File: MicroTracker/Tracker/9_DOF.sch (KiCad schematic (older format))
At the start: 6 parts

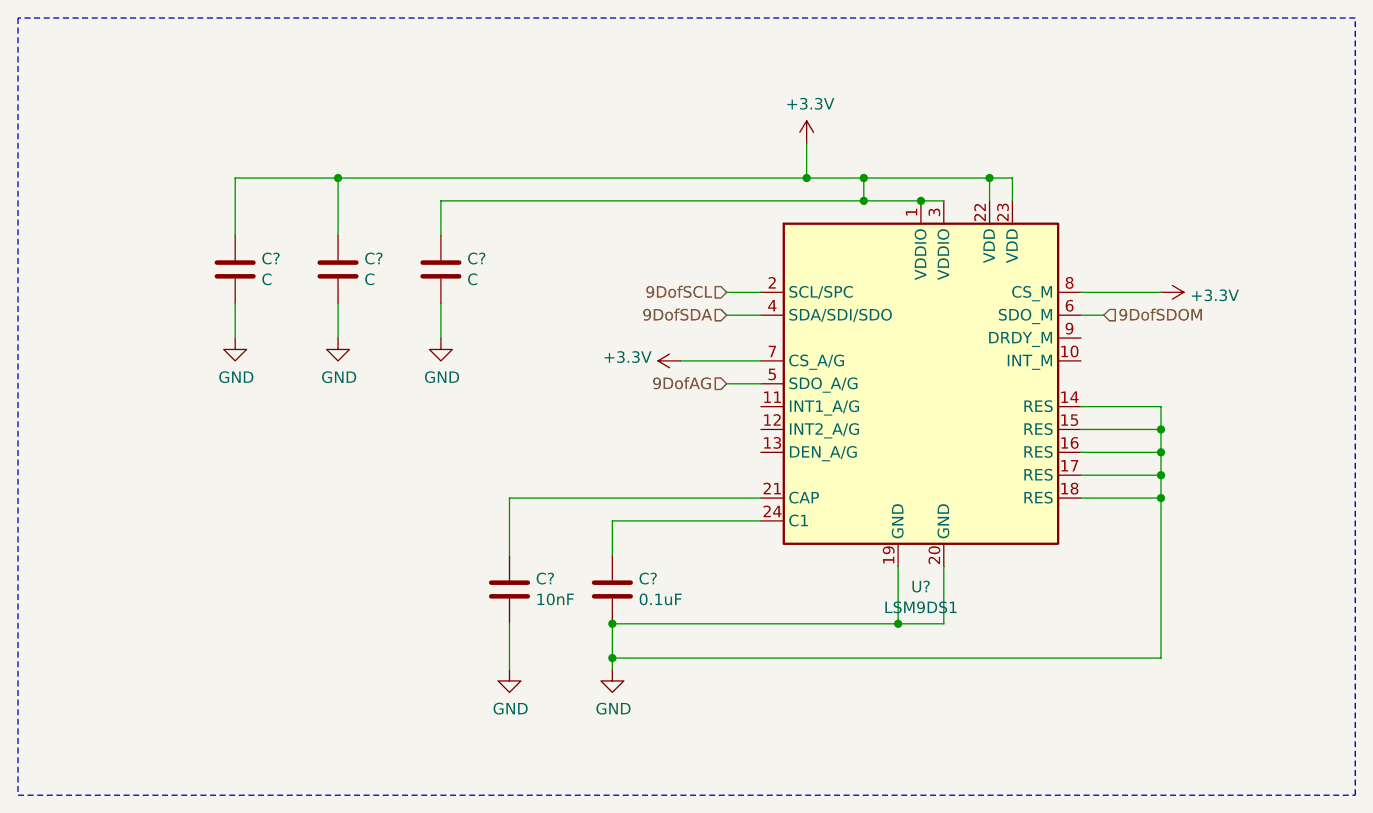
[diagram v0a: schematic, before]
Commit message: added charges
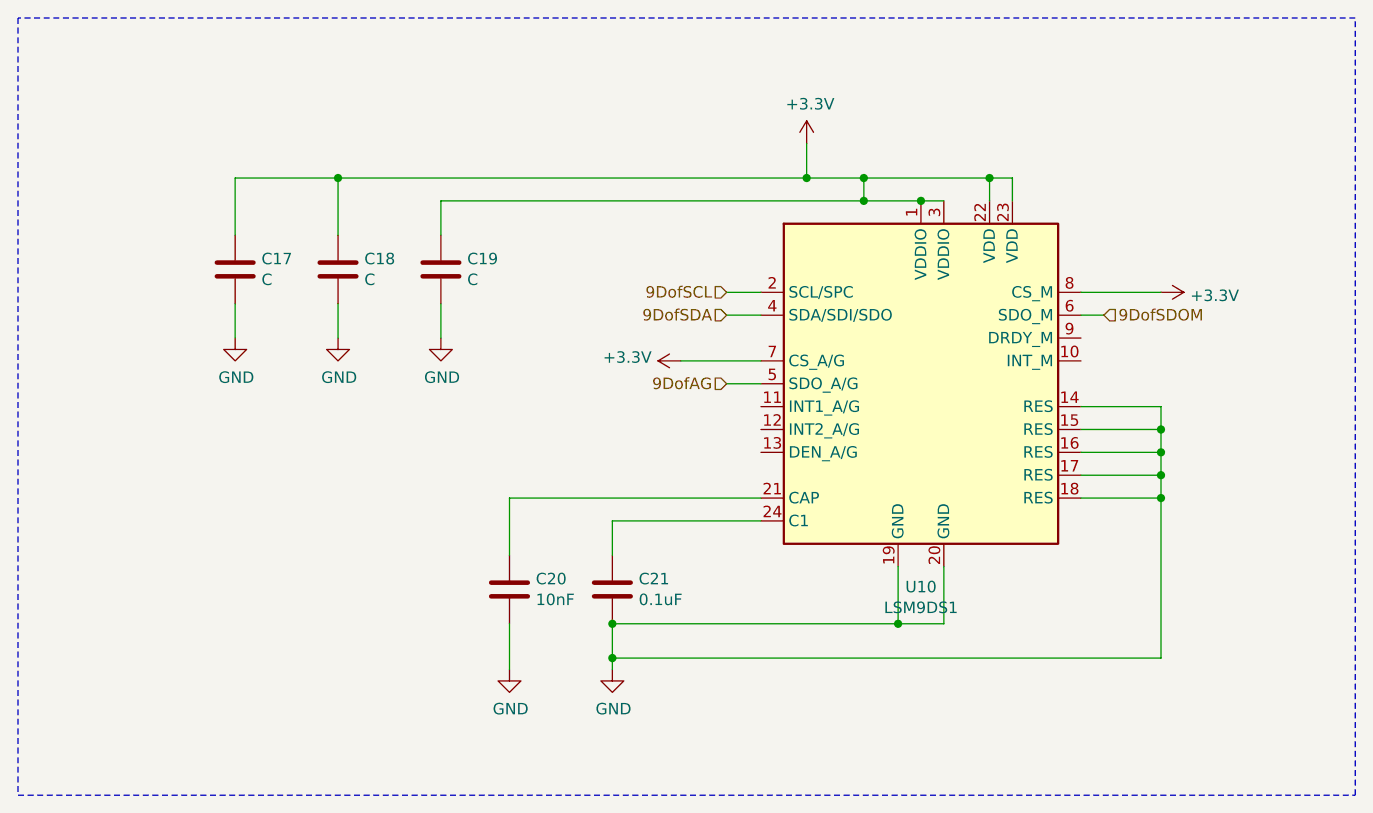
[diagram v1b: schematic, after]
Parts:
- gave numbers to parts that had none: 6
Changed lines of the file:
@@
 $EndDescr
 $Comp
-L Device:C C?
+L Device:C C18
 U 1 1 5F081816
 P 4150 3050
-F 0 "C?" H 4265 3096 50  0000 L CNN
+F 0 "C18" H 4265 3096 50  0000 L CNN
 F 1 "C" H 4265 3005 50  0000 L CNN
 F 2 "" H 4188 2900 50  0001 C CNN
@@
 $EndComp
 $Comp
-L Device:C C?
+L Device:C C19
 U 1 1 5F08223E
 P 4600 3050
-F 0 "C?" H 4715 3096 50  0000 L CNN
+F 0 "C19" H 4715 3096 50  0000 L CNN
 F 1 "C" H 4715 3005 50  0000 L CNN
 F 2 "" H 4638 2900 50  0001 C CNN
@@
 $EndComp
 $Comp
-L Device:C C?
+L Device:C C20
 U 1 1 5F08292F
 P 4900 4450
-F 0 "C?" H 5015 4496 50  0000 L CNN
+F 0 "C20" H 5015 4496 50  0000 L CNN
 F 1 "10nF" H 5015 4405 50  0000 L CNN
 F 2 "" H 4938 4300 50  0001 C CNN
@@
 $EndComp
 $Comp
-L Device:C C?
+L Device:C C21
 U 1 1 5F0833C0
 P 5350 4450
-F 0 "C?" H 5465 4496 50  0000 L CNN
+F 0 "C21" H 5465 4496 50  0000 L CNN
 F 1 "0.1uF" H 5465 4405 50  0000 L CNN
 F 2 "" H 5388 4300 50  0001 C CNN
@@
 $EndComp
 $Comp
-L Device:C C?
+L Device:C C17
 U 1 1 5F0838FF
 P 3700 3050
-F 0 "C?" H 3815 3096 50  0000 L CNN
+F 0 "C17" H 3815 3096 50  0000 L CNN
 F 1 "C" H 3815 3005 50  0000 L CNN
 F 2 "" H 3738 2900 50  0001 C CNN
@@
 	4900 4050 4900 4300
 $Comp
-L power:GND #PWR?
+L power:GND #PWR0157
 U 1 1 5F08A4FA
 P 4900 4800
-F 0 "#PWR?" H 4900 4550 50  0001 C CNN
+F 0 "#PWR0157" H 4900 4550 50  0001 C CNN
 F 1 "GND" H 4905 4627 50  0000 C CNN
 F 2 "" H 4900 4800 50  0001 C CNN
@@
 $EndComp
 $Comp
-L power:GND #PWR?
+L power:GND #PWR0158
 U 1 1 5F08AC1F
 P 5350 4800
-F 0 "#PWR?" H 5350 4550 50  0001 C CNN
+F 0 "#PWR0158" H 5350 4550 50  0001 C CNN
 F 1 "GND" H 5355 4627 50  0000 C CNN
 F 2 "" H 5350 4800 50  0001 C CNN
@@
 	6000 4150 5350 4150
 $Comp
-L Sensor_Motion:LSM9DS1 U?
+L Sensor_Motion:LSM9DS1 U10
 U 1 1 5F07FF21
 P 6700 3550
-F 0 "U?" H 6700 2661 50  0000 C CNN
+F 0 "U10" H 6700 2661 50  0000 C CNN
 F 1 "LSM9DS1" H 6700 2570 50  0000 C CNN
 F 2 "Package_LGA:LGA-24L_3x3.5mm_P0.43mm" H 8200 4300 50  0001 C CNN
@@
 	6600 4600 5350 4600
 $Comp
-L power:+3.3V #PWR?
+L power:+3.3V #PWR0159
 U 1 1 5F08DE33
 P 7750 3150
-F 0 "#PWR?" H 7750 3000 50  0001 C CNN
+F 0 "#PWR0159" H 7750 3000 50  0001 C CNN
 F 1 "+3.3V" V 7765 3278 50  0000 L CNN
 F 2 "" H 7750 3150 50  0001 C CNN
@@
 	7400 3150 7750 3150
 $Comp
-L power:+3.3V #PWR?
+L power:+3.3V #PWR0160
 U 1 1 5F090E2F
 P 5650 3450
-F 0 "#PWR?" H 5650 3300 50  0001 C CNN
+F 0 "#PWR0160" H 5650 3300 50  0001 C CNN
 F 1 "+3.3V" V 5665 3578 50  0000 L CNN
 F 2 "" H 5650 3450 50  0001 C CNN
@@
 	4150 2650 3700 2650
 $Comp
-L power:GND #PWR?
+L power:GND #PWR0161
 U 1 1 5F099576
 P 4600 3350
-F 0 "#PWR?" H 4600 3100 50  0001 C CNN
+F 0 "#PWR0161" H 4600 3100 50  0001 C CNN
 F 1 "GND" H 4605 3177 50  0000 C CNN
 F 2 "" H 4600 3350 50  0001 C CNN
@@
 $EndComp
 $Comp
-L power:GND #PWR?
+L power:GND #PWR0162
 U 1 1 5F099C04
 P 4150 3350
-F 0 "#PWR?" H 4150 3100 50  0001 C CNN
+F 0 "#PWR0162" H 4150 3100 50  0001 C CNN
 F 1 "GND" H 4155 3177 50  0000 C CNN
 F 2 "" H 4150 3350 50  0001 C CNN
@@
 $EndComp
 $Comp
-L power:GND #PWR?
+L power:GND #PWR0163
 U 1 1 5F09A29E
 P 3700 3350
-F 0 "#PWR?" H 3700 3100 50  0001 C CNN
+F 0 "#PWR0163" H 3700 3100 50  0001 C CNN
 F 1 "GND" H 3705 3177 50  0000 C CNN
 F 2 "" H 3700 3350 50  0001 C CNN
@@
 	6450 2650 6200 2650
 $Comp
-L power:+3.3V #PWR?
+L power:+3.3V #PWR0164
 U 1 1 5F09D5DF
 P 6200 2500
-F 0 "#PWR?" H 6200 2350 50  0001 C CNN
+F 0 "#PWR0164" H 6200 2350 50  0001 C CNN
 F 1 "+3.3V" H 6215 2673 50  0000 C CNN
 F 2 "" H 6200 2500 50  0001 C CNN

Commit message: assigned parts
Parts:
- C17, C18, C19, C20, C21: footprint (none) -> Capacitor_SMD:C_0805_2012Metric_Pad1.15x1.40mm_HandSolder
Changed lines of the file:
@@
 F 0 "C18" H 4265 3096 50  0000 L CNN
 F 1 "C" H 4265 3005 50  0000 L CNN
-F 2 "" H 4188 2900 50  0001 C CNN
+F 2 "Capacitor_SMD:C_0805_2012Metric_Pad1.15x1.40mm_HandSolder" H 4188 2900 50  0001 C CNN
 F 3 "~" H 4150 3050 50  0001 C CNN
 	1    4150 3050
@@
 F 0 "C19" H 4715 3096 50  0000 L CNN
 F 1 "C" H 4715 3005 50  0000 L CNN
-F 2 "" H 4638 2900 50  0001 C CNN
+F 2 "Capacitor_SMD:C_0805_2012Metric_Pad1.15x1.40mm_HandSolder" H 4638 2900 50  0001 C CNN
 F 3 "~" H 4600 3050 50  0001 C CNN
 	1    4600 3050
@@
 F 0 "C20" H 5015 4496 50  0000 L CNN
 F 1 "10nF" H 5015 4405 50  0000 L CNN
-F 2 "" H 4938 4300 50  0001 C CNN
+F 2 "Capacitor_SMD:C_0805_2012Metric_Pad1.15x1.40mm_HandSolder" H 4938 4300 50  0001 C CNN
 F 3 "~" H 4900 4450 50  0001 C CNN
 	1    4900 4450
@@
 F 0 "C21" H 5465 4496 50  0000 L CNN
 F 1 "0.1uF" H 5465 4405 50  0000 L CNN
-F 2 "" H 5388 4300 50  0001 C CNN
+F 2 "Capacitor_SMD:C_0805_2012Metric_Pad1.15x1.40mm_HandSolder" H 5388 4300 50  0001 C CNN
 F 3 "~" H 5350 4450 50  0001 C CNN
 	1    5350 4450
@@
 F 0 "C17" H 3815 3096 50  0000 L CNN
 F 1 "C" H 3815 3005 50  0000 L CNN
-F 2 "" H 3738 2900 50  0001 C CNN
+F 2 "Capacitor_SMD:C_0805_2012Metric_Pad1.15x1.40mm_HandSolder" H 3738 2900 50  0001 C CNN
 F 3 "~" H 3700 3050 50  0001 C CNN
 	1    3700 3050

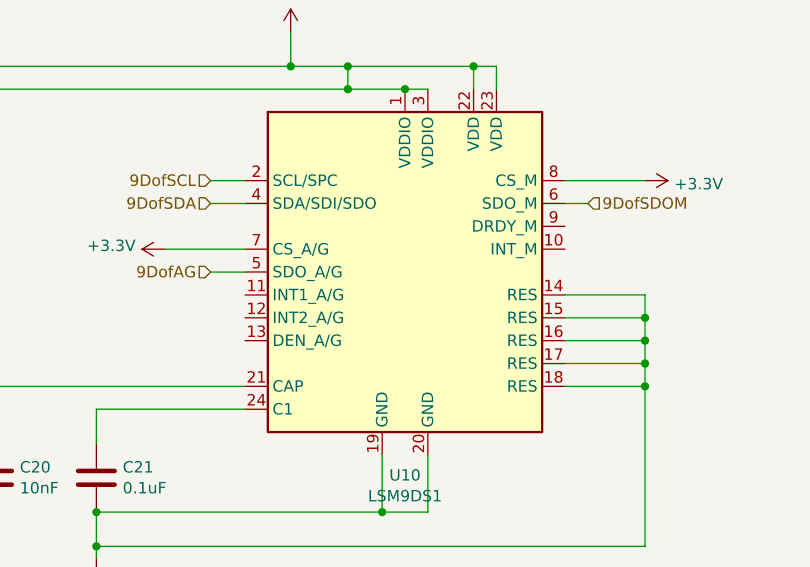
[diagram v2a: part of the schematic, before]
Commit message: added more parts and lib
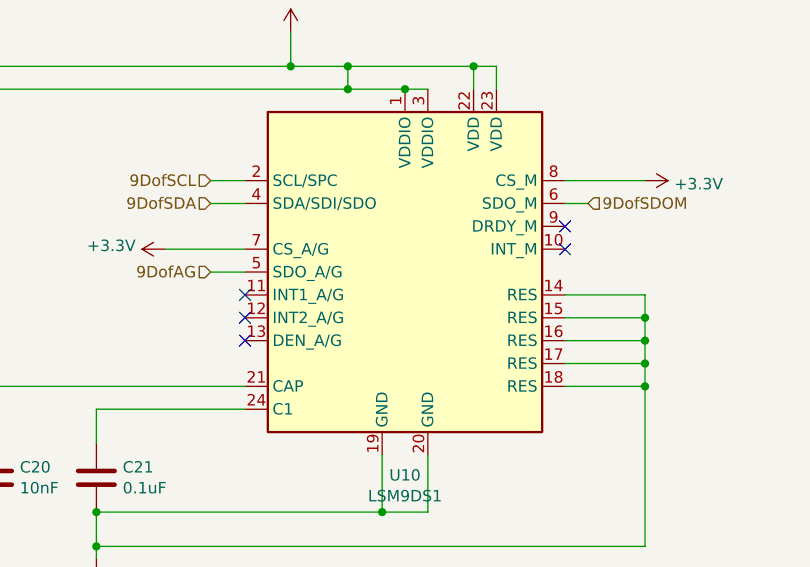
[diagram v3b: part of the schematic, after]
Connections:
- no-connect marks 0 -> 5
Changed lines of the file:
@@
 Wire Notes Line
 	2750 1950 2750 5350
+NoConn ~ 7400 3350
+NoConn ~ 7400 3450
+NoConn ~ 6000 3850
+NoConn ~ 6000 3750
+NoConn ~ 6000 3650
 $EndSCHEMATC
